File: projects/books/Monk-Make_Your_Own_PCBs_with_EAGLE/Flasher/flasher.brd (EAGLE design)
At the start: 78.7 x 61.9 mm, 10 parts, among them IC1 NE555, J1 1X2-3.5MM

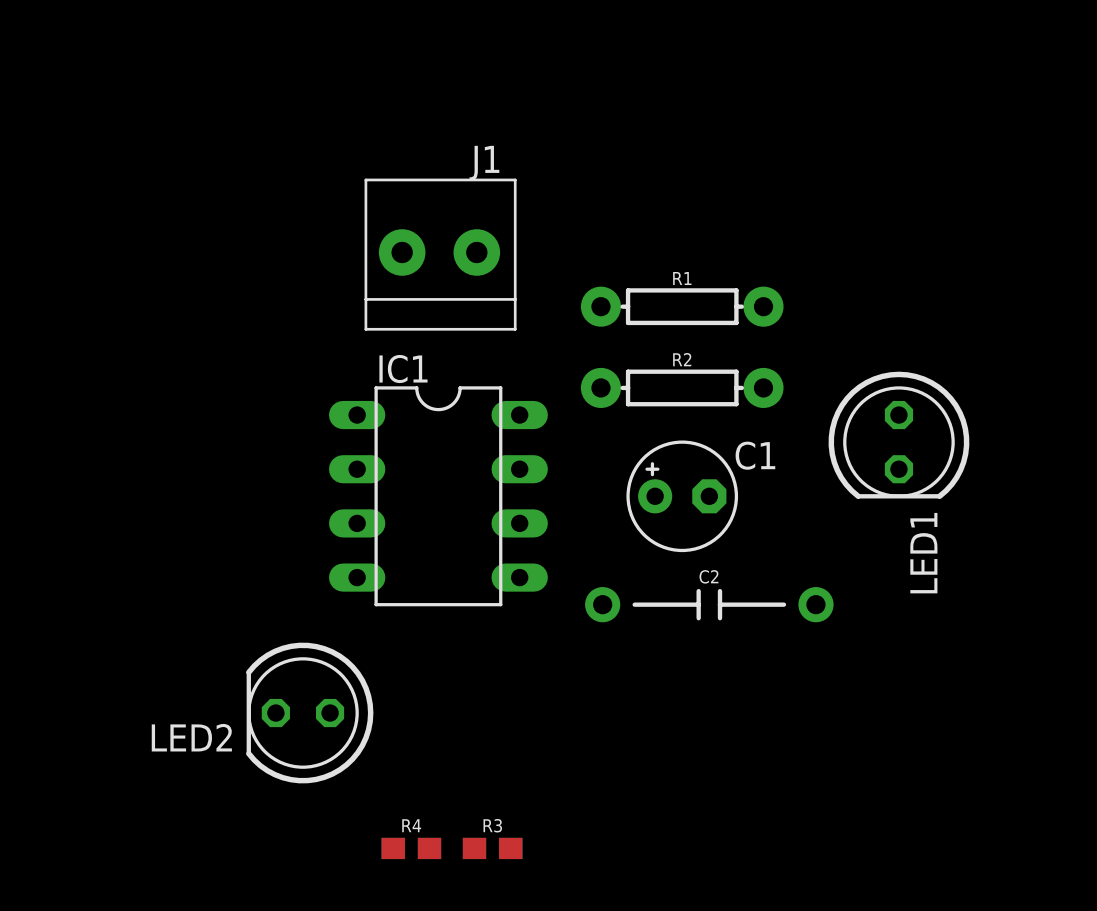
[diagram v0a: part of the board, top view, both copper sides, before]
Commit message: Updated placement of components of flasher board layout
Signed-off-by: Naveed Kawsar <naveedkawsar@outlook.com>
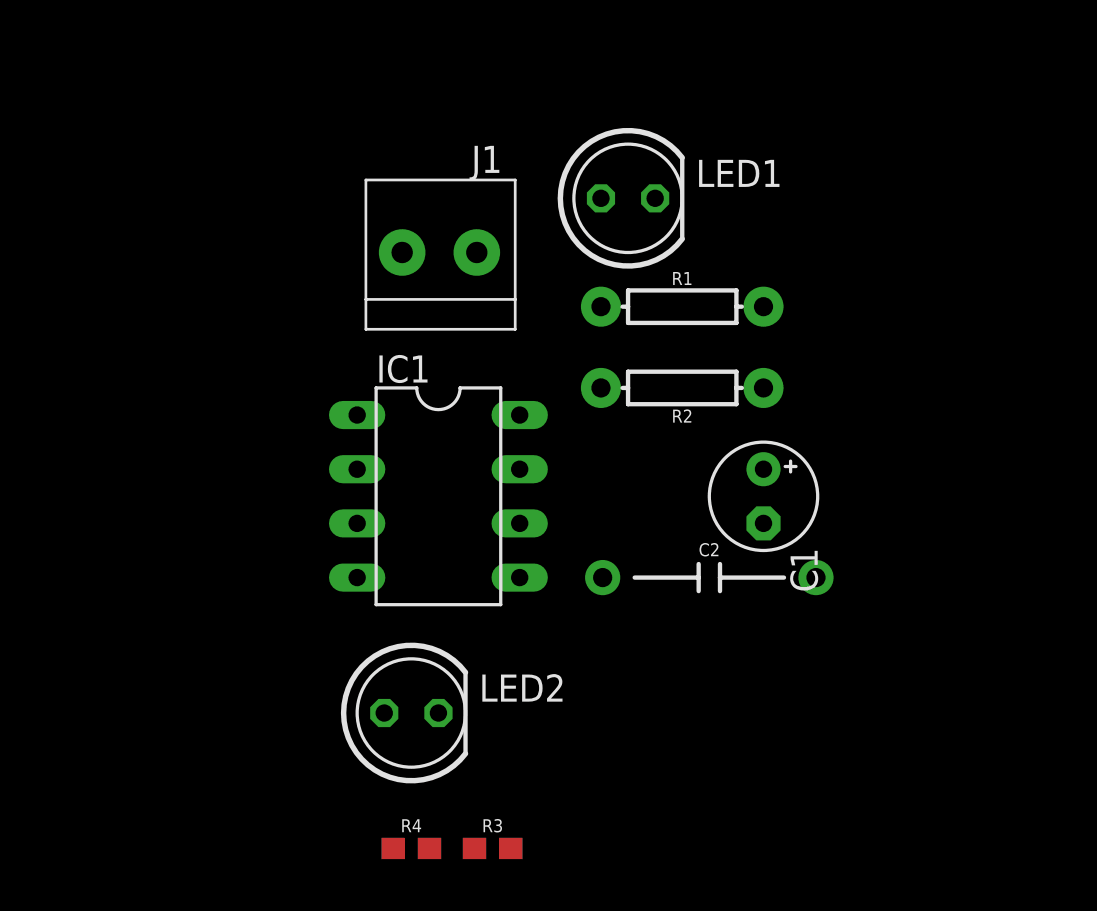
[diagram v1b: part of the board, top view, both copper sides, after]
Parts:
- moved LED1 17.1 mm to (76.2, 69.8), turned to 0 degrees
- moved LED2 5.08 mm to (66.0, 45.7), turned to 0 degrees
- moved C1 3.81 mm to (82.5, 55.9), turned to 270 degrees
- moved C2 1.27 mm to (80.0, 52.1)
- turned R2 to 180 degrees
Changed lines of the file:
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@@
 </autorouter>
 <elements>
-<element name="C1" library="resistor" library_urn="urn:adsk.eagle:library:348" package="E2,5-5" package3d_urn="urn:adsk.eagle:package:25841/1" value="1u" x="78.74" y="55.88"/>
-<element name="C2" library="SparkFun-Capacitors" package="CAP-PTH-10MM" value="10nF" x="80.01" y="50.8">
-<attribute name="PROD_ID" value="CAP-09321" x="80.01" y="50.8" size="1.778" layer="27" display="off"/>
+<element name="C1" library="resistor" library_urn="urn:adsk.eagle:library:348" package="E2,5-5" package3d_urn="urn:adsk.eagle:package:25841/1" value="1u" x="82.55" y="55.88" rot="R270"/>
+<element name="C2" library="SparkFun-Capacitors" package="CAP-PTH-10MM" value="10nF" x="80.01" y="52.07">
+<attribute name="PROD_ID" value="CAP-09321" x="80.01" y="52.07" size="1.778" layer="27" display="off"/>
 </element>
 <element name="IC1" library="st-microelectronics" library_urn="urn:adsk.eagle:library:368" package="DIL-08" package3d_urn="urn:adsk.eagle:package:26829/1" value="NE555" x="67.31" y="55.88" rot="R270">
@@
 </element>
 <element name="J1" library="adafruit" package="1X2-3.5MM" value="1X2-3.5MM" x="67.31" y="67.31"/>
-<element name="LED1" library="led" library_urn="urn:adsk.eagle:library:259" package="LED5MM" package3d_urn="urn:adsk.eagle:package:15799/1" value="Green" x="88.9" y="58.42" rot="R270"/>
-<element name="LED2" library="led" library_urn="urn:adsk.eagle:library:259" package="LED5MM" package3d_urn="urn:adsk.eagle:package:15799/1" value="Green" x="60.96" y="45.72" rot="R180"/>
+<element name="LED1" library="led" library_urn="urn:adsk.eagle:library:259" package="LED5MM" package3d_urn="urn:adsk.eagle:package:15799/1" value="Green" x="76.2" y="69.85"/>
+<element name="LED2" library="led" library_urn="urn:adsk.eagle:library:259" package="LED5MM" package3d_urn="urn:adsk.eagle:package:15799/1" value="Green" x="66.04" y="45.72"/>
 <element name="R1" library="SparkFun-Resistors" package="AXIAL-0.3" value="1k" x="78.74" y="64.77">
 <attribute name="PROD_ID" value="RES-12182" x="78.74" y="64.77" size="1.778" layer="27" display="off"/>
 </element>
-<element name="R2" library="SparkFun-Resistors" package="AXIAL-0.3" value=" 470k" x="78.74" y="60.96">
-<attribute name="PROD_ID" value=" " x="78.74" y="60.96" size="1.778" layer="27" display="off"/>
+<element name="R2" library="SparkFun-Resistors" package="AXIAL-0.3" value=" 470k" x="78.74" y="60.96" rot="R180">
+<attribute name="PROD_ID" value=" " x="78.74" y="60.96" size="1.778" layer="27" rot="R180" display="off"/>
 </element>
 <element name="R3" library="SparkFun-Resistors" package="0603" value="220" x="69.85" y="39.37">
@@
 <contactref element="LED1" pad="K"/>
 <contactref element="R3" pad="2"/>
-<wire x1="88.9" y1="57.15" x2="70.7" y2="39.37" width="0" layer="19" extent="1-1"/>
+<wire x1="77.47" y1="69.85" x2="70.7" y2="39.37" width="0" layer="19" extent="1-1"/>
 </signal>
 <signal name="N$2">
@@
 <contactref element="R1" pad="P$1"/>
 <contactref element="R2" pad="P$2"/>
-<wire x1="74.93" y1="64.77" x2="82.55" y2="60.96" width="0" layer="19" extent="1-1"/>
+<wire x1="74.93" y1="64.77" x2="74.93" y2="60.96" width="0" layer="19" extent="1-1"/>
 <wire x1="71.12" y1="57.15" x2="74.93" y2="64.77" width="0" layer="19" extent="1-1"/>
 </signal>
@@
 <contactref element="IC1" pad="2"/>
 <wire x1="71.12" y1="54.61" x2="63.5" y2="57.15" width="0" layer="19" extent="1-1"/>
-<wire x1="77.47" y1="55.88" x2="71.12" y2="54.61" width="0" layer="19" extent="1-1"/>
-<wire x1="74.93" y1="60.96" x2="77.47" y2="55.88" width="0" layer="19" extent="1-1"/>
+<wire x1="82.55" y1="57.15" x2="71.12" y2="54.61" width="0" layer="19" extent="1-1"/>
+<wire x1="82.55" y1="60.96" x2="82.55" y2="57.15" width="0" layer="19" extent="1-1"/>
 </signal>
 <signal name="N$7">
 <contactref element="LED2" pad="A"/>
 <contactref element="R4" pad="1"/>
-<wire x1="65.19" y1="39.37" x2="62.23" y2="45.72" width="0" layer="19" extent="1-1"/>
+<wire x1="65.19" y1="39.37" x2="64.77" y2="45.72" width="0" layer="19" extent="1-1"/>
 </signal>
 <signal name="VCC+">
@@
 <contactref element="J1" pad="1"/>
 <wire x1="71.12" y1="59.69" x2="69.11" y2="67.31" width="0" layer="19" extent="1-1"/>
-<wire x1="88.9" y1="59.69" x2="71.12" y2="59.69" width="0" layer="19" extent="1-1"/>
-<wire x1="82.55" y1="64.77" x2="88.9" y2="59.69" width="0" layer="19" extent="1-1"/>
+<wire x1="74.93" y1="69.85" x2="71.12" y2="59.69" width="0" layer="19" extent="1-1"/>
+<wire x1="82.55" y1="64.77" x2="74.93" y2="69.85" width="0" layer="19" extent="1-1"/>
 <wire x1="63.5" y1="52.07" x2="71.12" y2="59.69" width="0" layer="19" extent="1-1"/>
 </signal>
@@
 <contactref element="IC1" pad="5"/>
 <contactref element="C2" pad="1"/>
-<wire x1="75.01" y1="50.8" x2="71.12" y2="52.07" width="0" layer="19" extent="1-1"/>
+<wire x1="75.01" y1="52.07" x2="71.12" y2="52.07" width="0" layer="19" extent="1-1"/>
 </signal>
 <signal name="GND">
@@
 <contactref element="C2" pad="2"/>
 <wire x1="63.5" y1="59.69" x2="65.61" y2="67.31" width="0" layer="19" extent="1-1"/>
-<wire x1="59.69" y1="45.72" x2="65.61" y2="67.31" width="0" layer="19" extent="1-1"/>
-<wire x1="85.01" y1="50.8" x2="59.69" y2="45.72" width="0" layer="19" extent="1-1"/>
-<wire x1="80.01" y1="55.88" x2="85.01" y2="50.8" width="0" layer="19" extent="1-1"/>
+<wire x1="67.31" y1="45.72" x2="65.61" y2="67.31" width="0" layer="19" extent="1-1"/>
+<wire x1="85.01" y1="52.07" x2="67.31" y2="45.72" width="0" layer="19" extent="1-1"/>
+<wire x1="82.55" y1="54.61" x2="85.01" y2="52.07" width="0" layer="19" extent="1-1"/>
 </signal>
 </signals>
